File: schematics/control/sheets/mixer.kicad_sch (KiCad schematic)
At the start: 29 parts, among them U1 TL074, U5 TL074

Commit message: Added pulse width mod schematics
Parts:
- renumbered C6 to C1, C8 to C2, C7 to C3, C9 to C4, C11 to C5, C4 to C6, C5 to C7, R7 to R10, R10 to R11, R11 to R12, R12 to R13, R13 to R14, R14 to R15, R15 to R16, R1 to R17, R53 to R18, R8 to R19, R54 to R20, R9 to R21, R59 to R22, R58 to R23, R2 to R5, R3 to R6, R4 to R7, R5 to R8, R6 to R9, U1 to U4, U5 to U4

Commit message: Updated VCA
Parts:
- added TP_SAW_SUBMIX1, TP_SQR_SUBMIX1, TP_V_SAW1, TP_V_SAW2, TP_V_SAW3, TP_V_SAW4, TP_V_SAW5, TP_V_SAW6, TP_V_SQR1, TP_V_SQR2, TP_V_SQR3, TP_V_SQR4, TP_V_SQR5, TP_V_SQR6: TestPoint, symbol Connector:TestPoint
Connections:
- net SAW_1_IN: now also TP_V_SAW1.1
- net SAW_2_IN: now also TP_V_SAW2.1
- net SAW_3_IN: now also TP_V_SAW3.1
- net SAW_4_IN: now also TP_V_SAW4.1
- net SAW_5_IN: now also TP_V_SAW5.1
- net SAW_6_IN: now also TP_V_SAW6.1
- net SQR_1_IN: now also TP_V_SQR1.1
- net SQR_2_IN: now also TP_V_SQR2.1
- net SQR_3_IN: now also TP_V_SQR3.1
- net SQR_4_IN: now also TP_V_SQR4.1
- net SQR_5_IN: now also TP_V_SQR5.1
- net SQR_6_IN: now also TP_V_SQR6.1
- net at C3.2, R21.2, SW_SQR_SAW1.1 (A)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: now also TP_SAW_SUBMIX1.1
- net at C4.2, R22.2, SW_SQR_SAW1.3 (C)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: now also TP_SQR_SUBMIX1.1
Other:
- moved on the sheet: C1, C2, C3, C4, C5, R10, R11, R12, R13, R14, R15, R16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

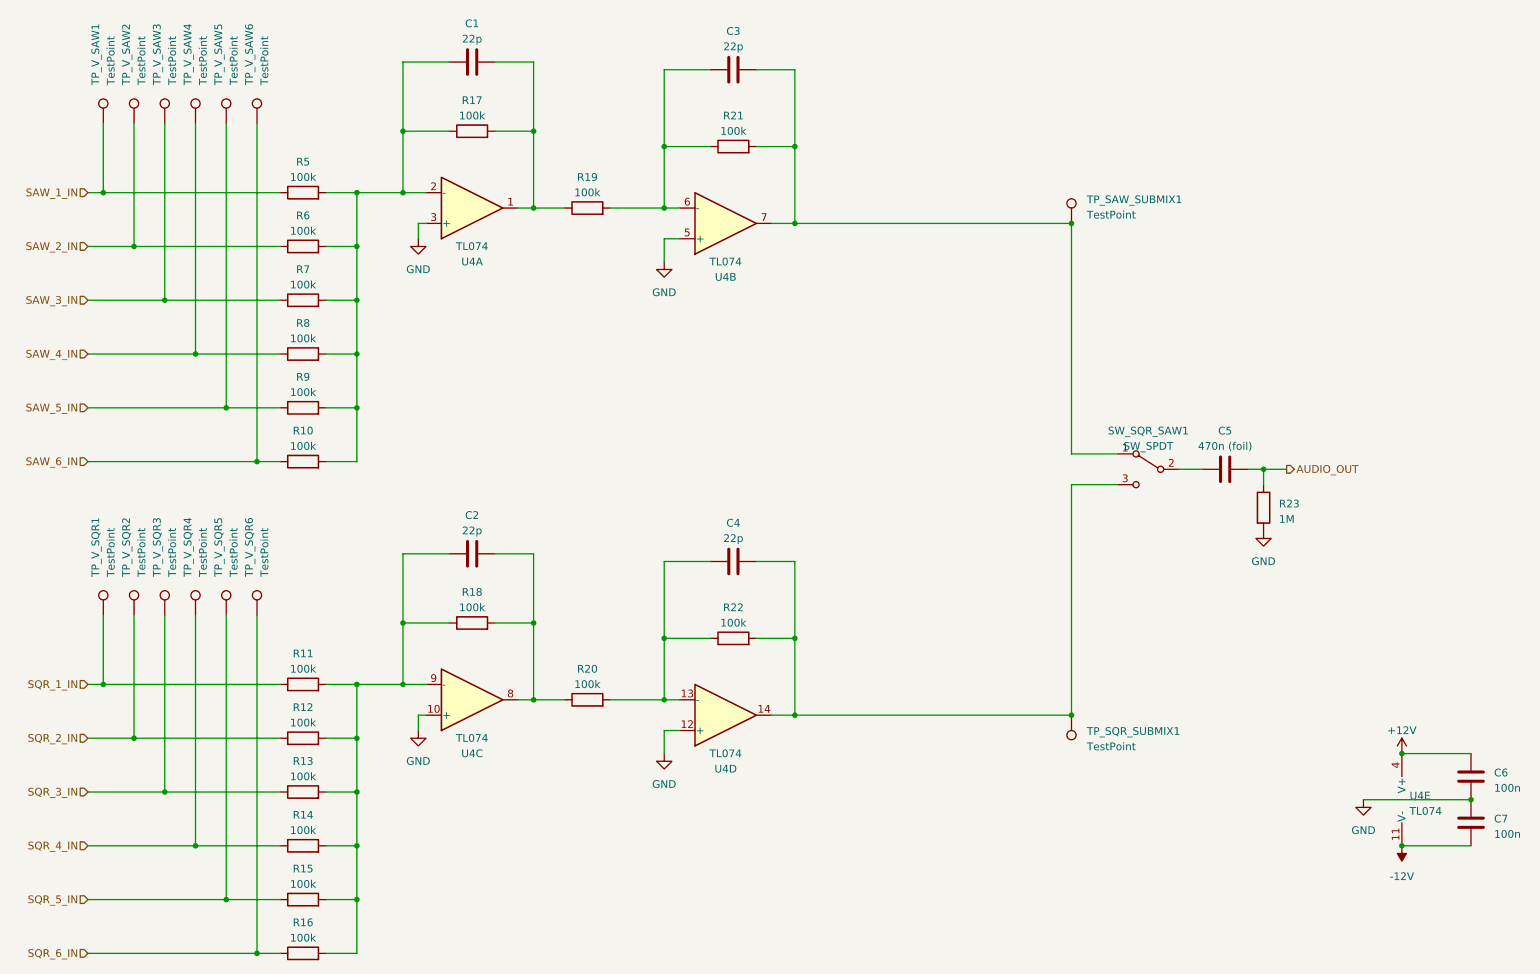
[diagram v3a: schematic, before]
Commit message: Added all UI components to schematics
- digital UI
- filter UI
- updated voice interface connection
- simplified schematics a lot
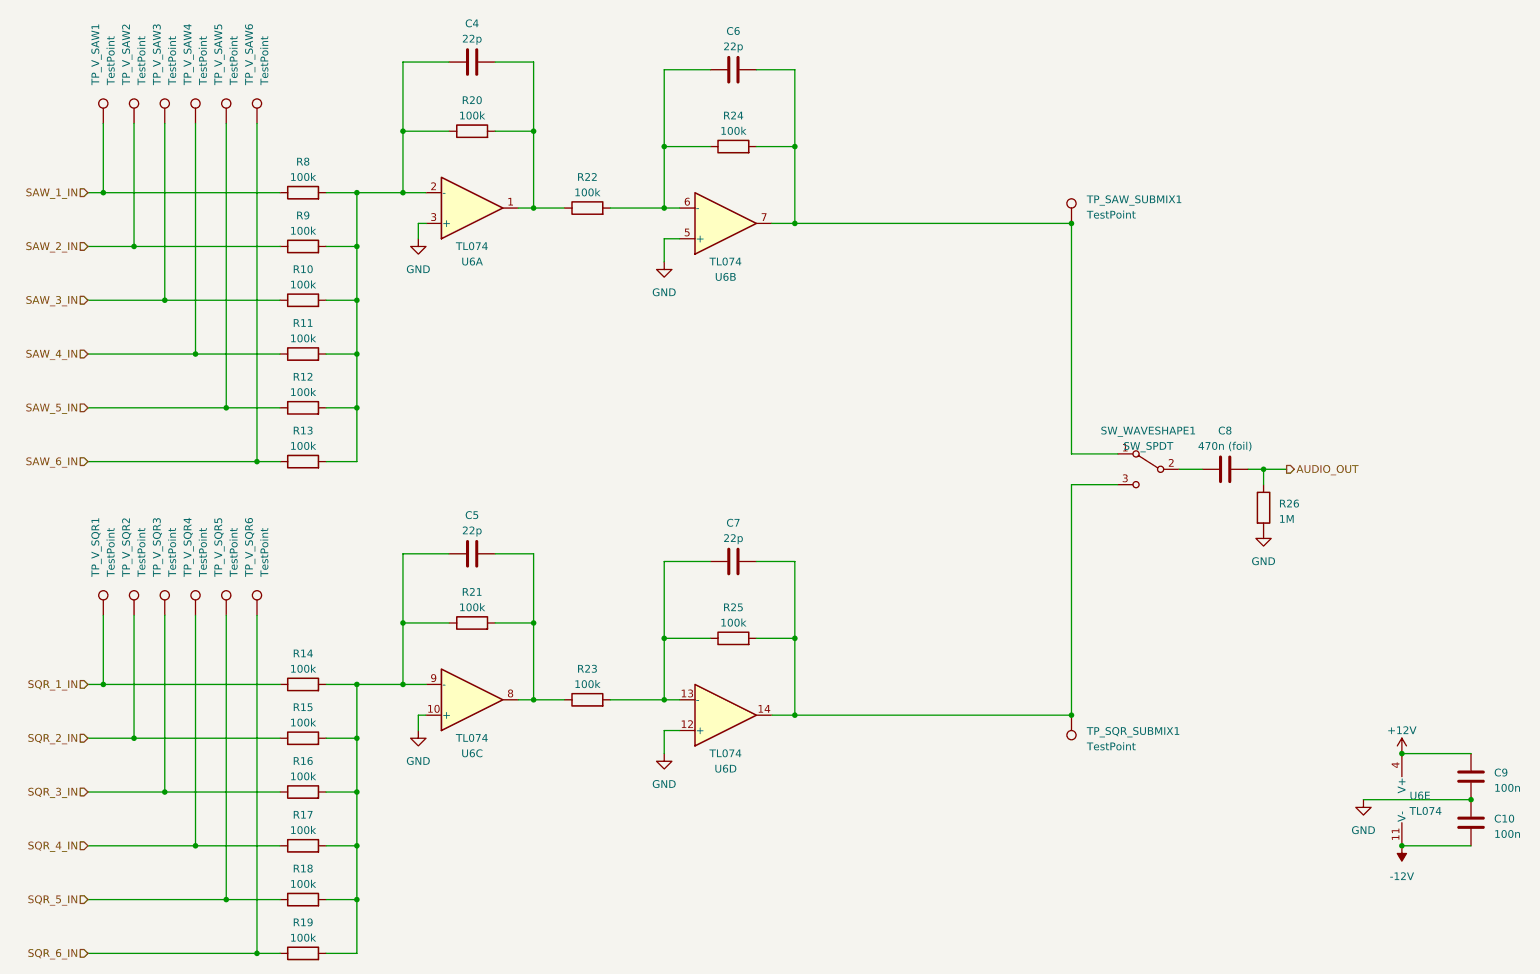
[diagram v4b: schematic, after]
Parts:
- C10: renamed from C7; footprint Capacitor_THT:C_Disc_D3.0mm_W2.0mm_P2.50mm -> (none)
- C4: renamed from C1; footprint Capacitor_THT:C_Disc_D3.0mm_W2.0mm_P2.50mm -> (none)
- C5: renamed from C2; footprint Capacitor_THT:C_Disc_D3.0mm_W2.0mm_P2.50mm -> (none)
- C6: renamed from C3; footprint Capacitor_THT:C_Disc_D3.0mm_W2.0mm_P2.50mm -> (none)
- C7: renamed from C4; footprint Capacitor_THT:C_Disc_D3.0mm_W2.0mm_P2.50mm -> (none)
- C8: renamed from C5; footprint Capacitor_THT:C_Rect_L7.2mm_W3.5mm_P5.00mm_FKS2_FKP2_MKS2_MKP2 -> (none)
- C9: renamed from C6; footprint Capacitor_THT:C_Disc_D3.0mm_W2.0mm_P2.50mm -> (none)
- R10: renamed from R7; footprint Shmoergh_Custom_Footprints:R_Axial_DIN0207_L6.3mm_D2.5mm_P7.62mm_Horizontal -> (none)
- R11: renamed from R8; footprint Shmoergh_Custom_Footprints:R_Axial_DIN0207_L6.3mm_D2.5mm_P7.62mm_Horizontal -> (none)
- R12: renamed from R9; footprint Shmoergh_Custom_Footprints:R_Axial_DIN0207_L6.3mm_D2.5mm_P7.62mm_Horizontal -> (none)
- R13: renamed from R10; footprint Shmoergh_Custom_Footprints:R_Axial_DIN0207_L6.3mm_D2.5mm_P7.62mm_Horizontal -> (none)
- R14: renamed from R11; footprint Shmoergh_Custom_Footprints:R_Axial_DIN0207_L6.3mm_D2.5mm_P7.62mm_Horizontal -> (none)
- R15: renamed from R12; footprint Shmoergh_Custom_Footprints:R_Axial_DIN0207_L6.3mm_D2.5mm_P7.62mm_Horizontal -> (none)
- R16: renamed from R13; footprint Shmoergh_Custom_Footprints:R_Axial_DIN0207_L6.3mm_D2.5mm_P7.62mm_Horizontal -> (none)
- R17: renamed from R14; footprint Shmoergh_Custom_Footprints:R_Axial_DIN0207_L6.3mm_D2.5mm_P7.62mm_Horizontal -> (none)
- R18: renamed from R15; footprint Shmoergh_Custom_Footprints:R_Axial_DIN0207_L6.3mm_D2.5mm_P7.62mm_Horizontal -> (none)
- R19: renamed from R16; footprint Shmoergh_Custom_Footprints:R_Axial_DIN0207_L6.3mm_D2.5mm_P7.62mm_Horizontal -> (none)
- R20: renamed from R17; footprint Shmoergh_Custom_Footprints:R_Axial_DIN0207_L6.3mm_D2.5mm_P7.62mm_Horizontal -> (none)
- R21: renamed from R18; footprint Shmoergh_Custom_Footprints:R_Axial_DIN0207_L6.3mm_D2.5mm_P7.62mm_Horizontal -> (none)
- R22: renamed from R19; footprint Shmoergh_Custom_Footprints:R_Axial_DIN0207_L6.3mm_D2.5mm_P7.62mm_Horizontal -> (none)
- R23: renamed from R20; footprint Shmoergh_Custom_Footprints:R_Axial_DIN0207_L6.3mm_D2.5mm_P7.62mm_Horizontal -> (none)
- R24: renamed from R21; footprint Shmoergh_Custom_Footprints:R_Axial_DIN0207_L6.3mm_D2.5mm_P7.62mm_Horizontal -> (none)
- R25: renamed from R22; footprint Shmoergh_Custom_Footprints:R_Axial_DIN0207_L6.3mm_D2.5mm_P7.62mm_Horizontal -> (none)
- R26: renamed from R23; footprint Shmoergh_Custom_Footprints:R_Axial_DIN0207_L6.3mm_D2.5mm_P7.62mm_Horizontal -> (none)
- R8: renamed from R5; footprint Shmoergh_Custom_Footprints:R_Axial_DIN0207_L6.3mm_D2.5mm_P7.62mm_Horizontal -> (none)
- R9: renamed from R6; footprint Shmoergh_Custom_Footprints:R_Axial_DIN0207_L6.3mm_D2.5mm_P7.62mm_Horizontal -> (none)
- renumbered SW_SQR_SAW1 to SW_WAVESHAPE1, U4 to U6

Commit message: Schemo work
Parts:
- removed TP_V_SAW1, TP_V_SAW2, TP_V_SAW3, TP_V_SAW4, TP_V_SAW5, TP_V_SAW6, TP_V_SQR1, TP_V_SQR2, TP_V_SQR3, TP_V_SQR4, TP_V_SQR5, TP_V_SQR6: TestPoint, symbol Connector:TestPoint
- C10, C4, C5, C6, C7, C9: footprint (none) -> Capacitor_THT:C_Disc_D3.0mm_W2.0mm_P2.50mm
- C8: footprint (none) -> Capacitor_THT:C_Rect_L7.0mm_W3.5mm_P5.00mm
- R10, R11, R12, R13, R14, R15, R16, R17, R18, R19, R20, R21, R22, R23, R24, R25, R26, R8, R9: footprint (none) -> Shmoergh_Custom_Footprints:R_Axial_DIN0207_L6.3mm_D2.5mm_P7.62mm_Horizontal
- SW_WAVESHAPE1: footprint (none) -> Shmoergh_Custom_Footprints:NSL25_01x03_Vertical
- TP_SAW_SUBMIX1, TP_SQR_SUBMIX1: footprint (none) -> TestPoint:TestPoint_THTPad_D2.0mm_Drill1.0mm
- U6: footprint (none) -> PCM_Package_DIP_AKL:DIP-14_W7.62mm_LongPads
